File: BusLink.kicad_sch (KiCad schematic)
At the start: 3 parts, among them J1 DE9_Pins, U1 STM32H723VETx, U2 USB3300-EZK

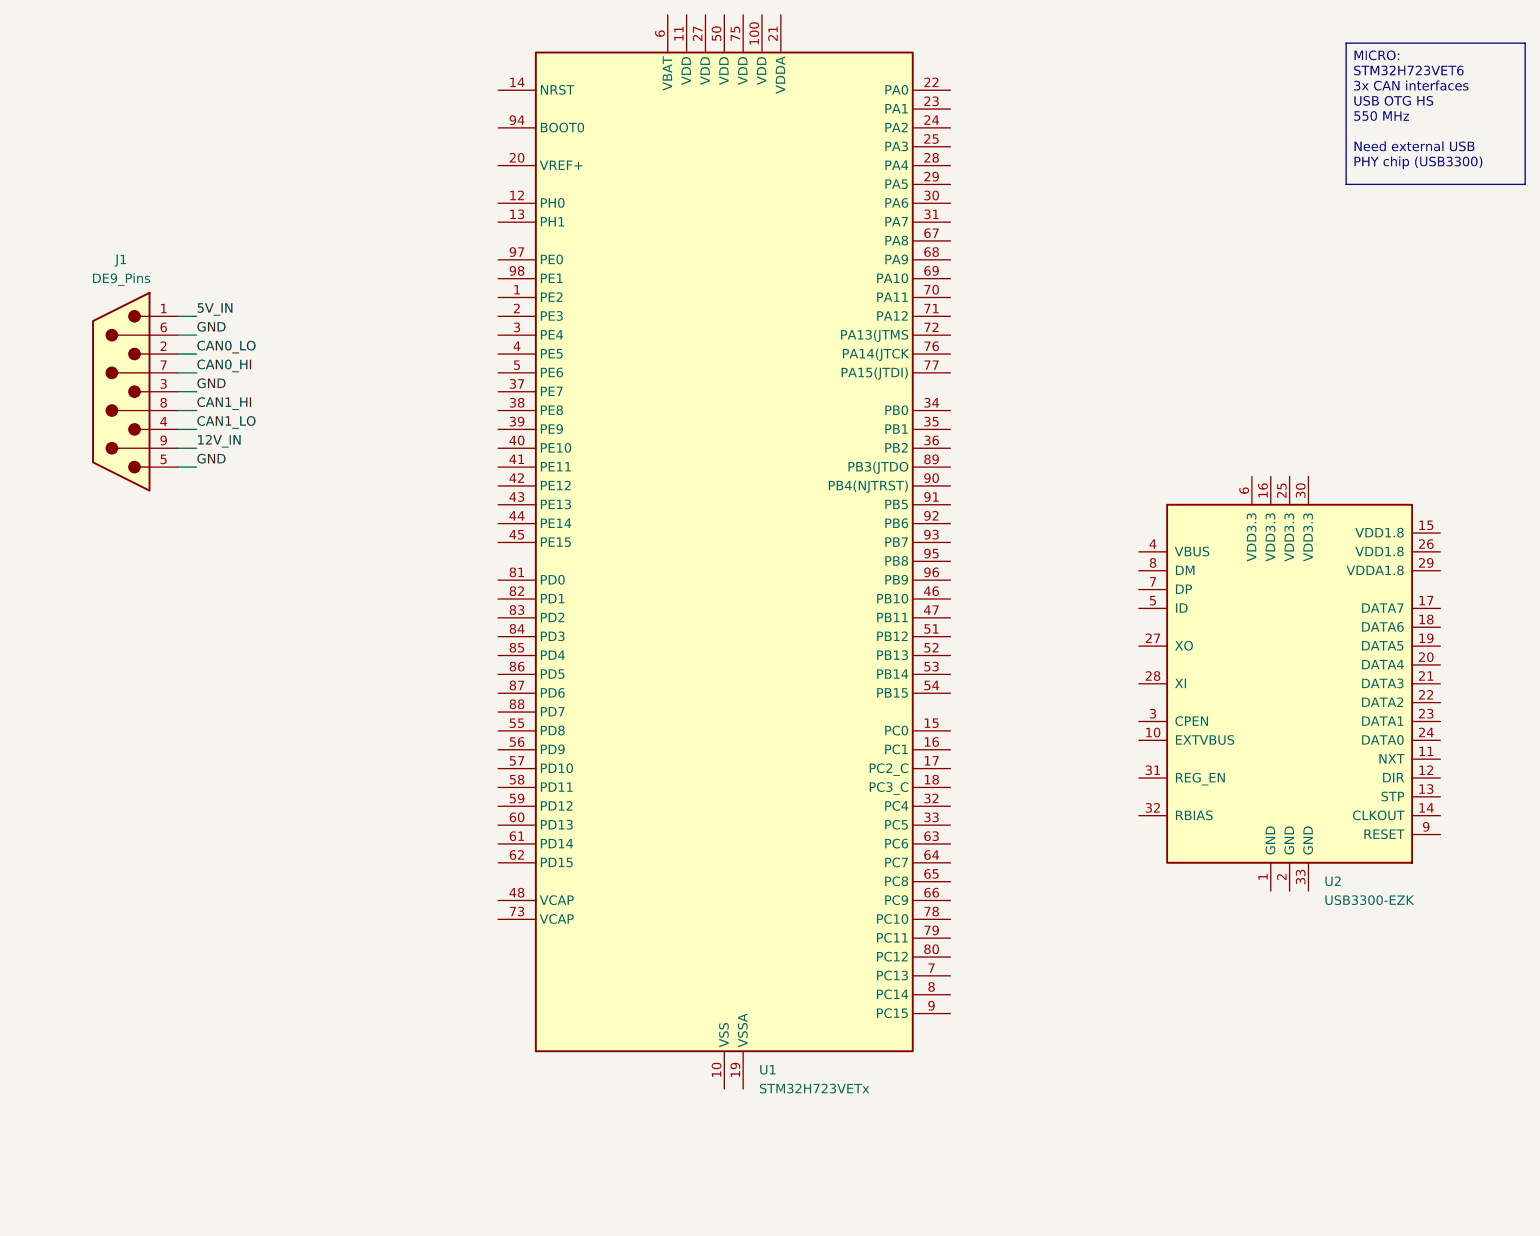
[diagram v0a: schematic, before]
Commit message: setting up heirarchy
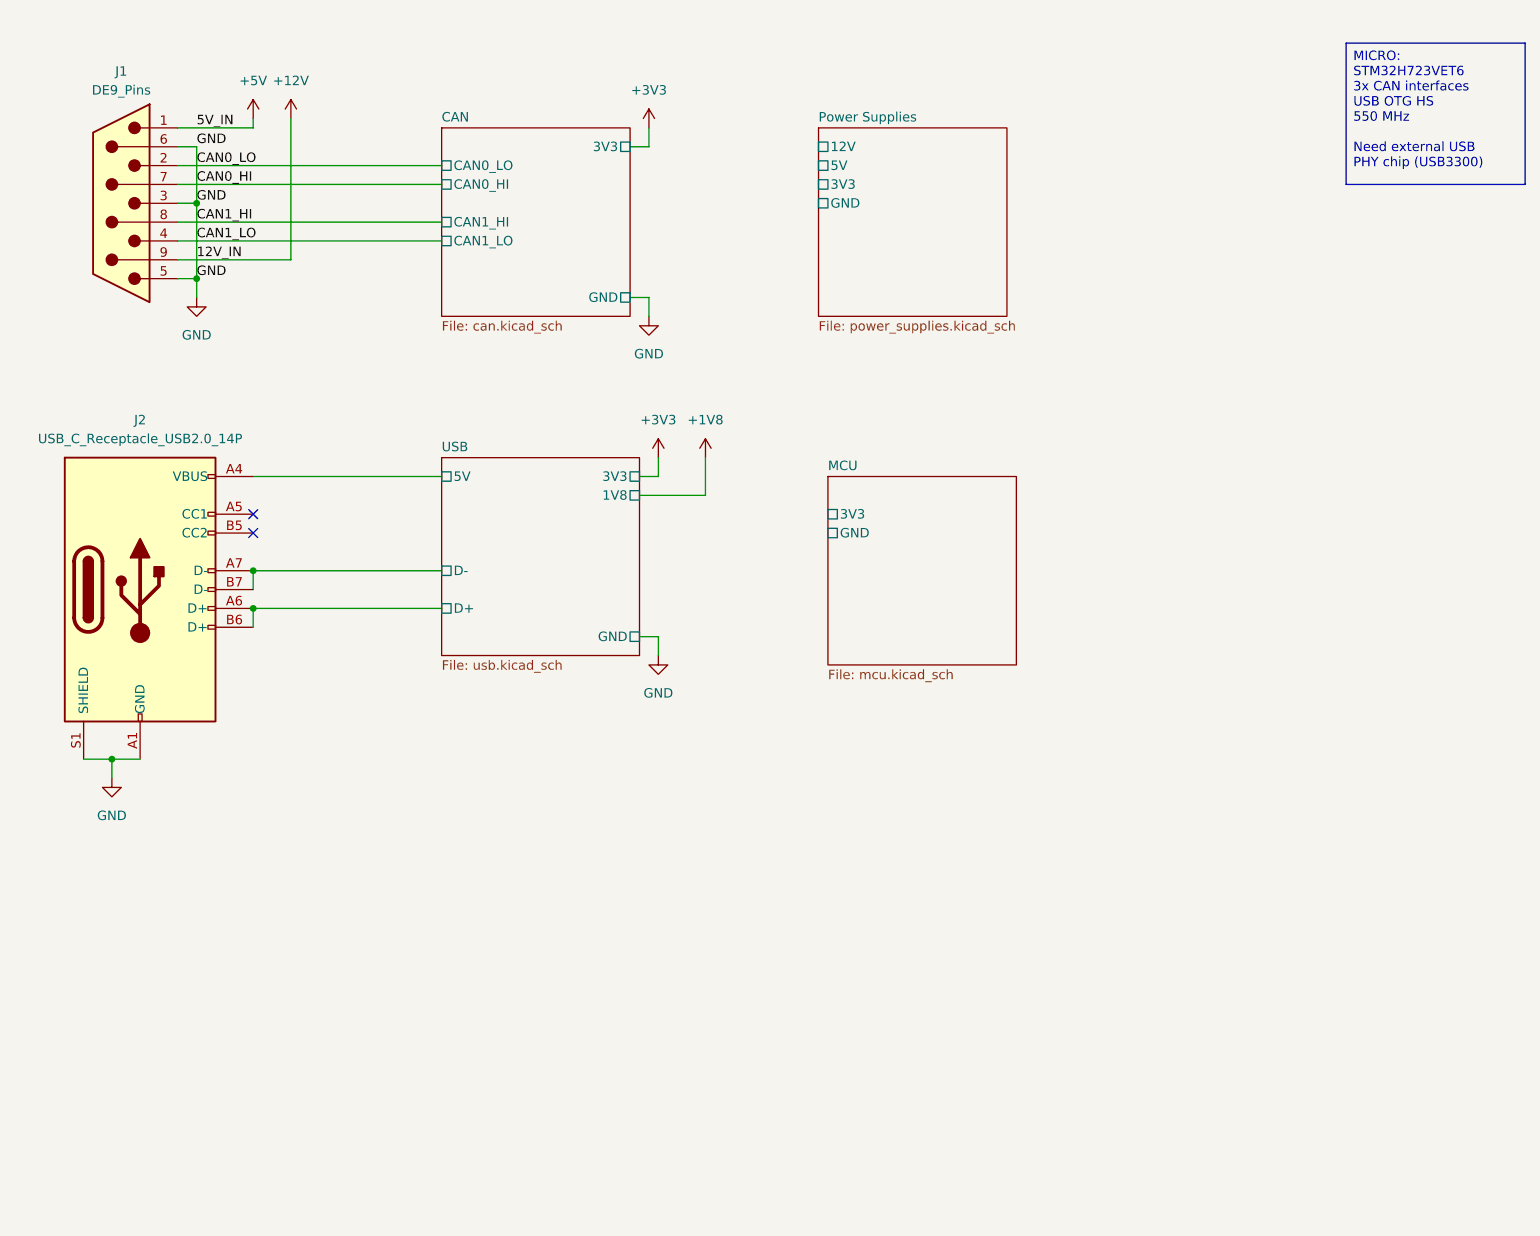
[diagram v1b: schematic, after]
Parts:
- removed U1: STM32H723VETx, Package_QFP:LQFP-100_14x14mm_P0.5mm, symbol MCU_ST_STM32H7:STM32H723VETx
- removed U2: USB3300-EZK, Package_DFN_QFN:QFN-32-1EP_5x5mm_P0.5mm_EP3.45x3.45mm, symbol Interface_USB:USB3300-EZK
- added J2: USB_C_Receptacle_USB2.0_14P, Connector_USB:USB_C_Receptacle_GCT_USB4110, symbol Connector:USB_C_Receptacle_USB2.0_14P
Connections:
- net CAN0_HI is gone; now on net +12V: J1.7
- net CAN0_LO is gone; now on net +12V: J1.2
- net CAN1_HI is gone; now on net +12V: J1.8
- net CAN1_LO is gone; now on net +12V: J1.4
- net GND is gone; now on net +12V: J1.3, J1.5, J1.6
- net 12V_IN renamed +12V
- net +12V: now also J2.A1 (GND), J2.A12 (GND), J2.B1 (GND), J2.B12 (GND), J2.S1 (SHIELD)
- net 5V_IN renamed +5V
- new net USB/5V: J2.A4 (VBUS), J2.A9 (VBUS), J2.B4 (VBUS), J2.B9 (VBUS)
- new net USB/D+: J2.A6 (D+), J2.B6 (D+)
- new net USB/D-: J2.A7 (D-), J2.B7 (D-)
- no-connect marks 0 -> 2
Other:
- added sheet CAN (can.kicad_sch)
- added sheet MCU (mcu.kicad_sch)
- added sheet Power Supplies (power_supplies.kicad_sch)
- added sheet USB (usb.kicad_sch)
- moved on the sheet: J1

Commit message: working on power supplies and CAN
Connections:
- net USB/5V is gone; now on net +5V: J2.A4 (VBUS), J2.A9 (VBUS), J2.B4 (VBUS), J2.B9 (VBUS)
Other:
- sheet CAN ports: added CAN0_RX, CAN0_TX, CAN1_RX, CAN1_TX; removed none
- sheet MCU ports: added CAN0_RX, CAN0_TX, CAN1_RX, CAN1_TX; removed none
- sheet Power Supplies: file power_supplies.kicad_sch -> pwr.kicad_sch
- sheet Power Supplies ports: added 1V8; removed none
